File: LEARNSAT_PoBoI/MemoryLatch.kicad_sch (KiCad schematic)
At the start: 1 part, among them U23 SN74LVC1G373DCKR

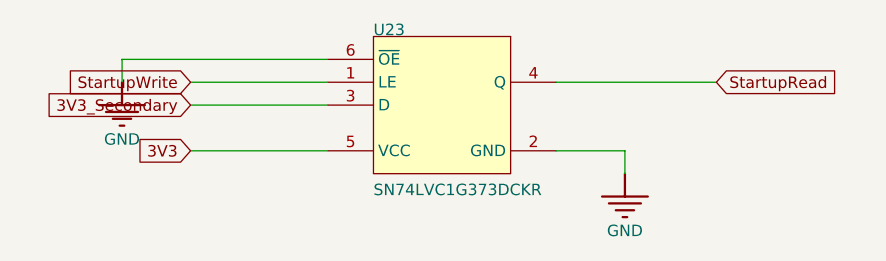
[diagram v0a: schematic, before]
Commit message: Added footprints
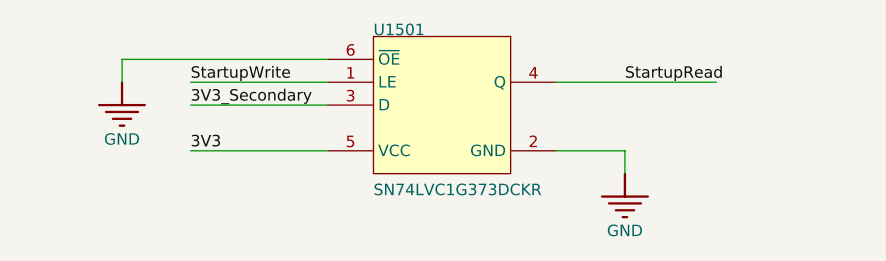
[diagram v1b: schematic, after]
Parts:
- U1501: renamed from U23; footprint DCK0006A_M -> SN74LVC1G373DCKR:SOT65P210X110-6N
